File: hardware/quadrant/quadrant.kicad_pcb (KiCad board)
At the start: 4 copper layers, 216 x 200 mm, 68 parts, among them J1 FPC 16, P1 NPTH

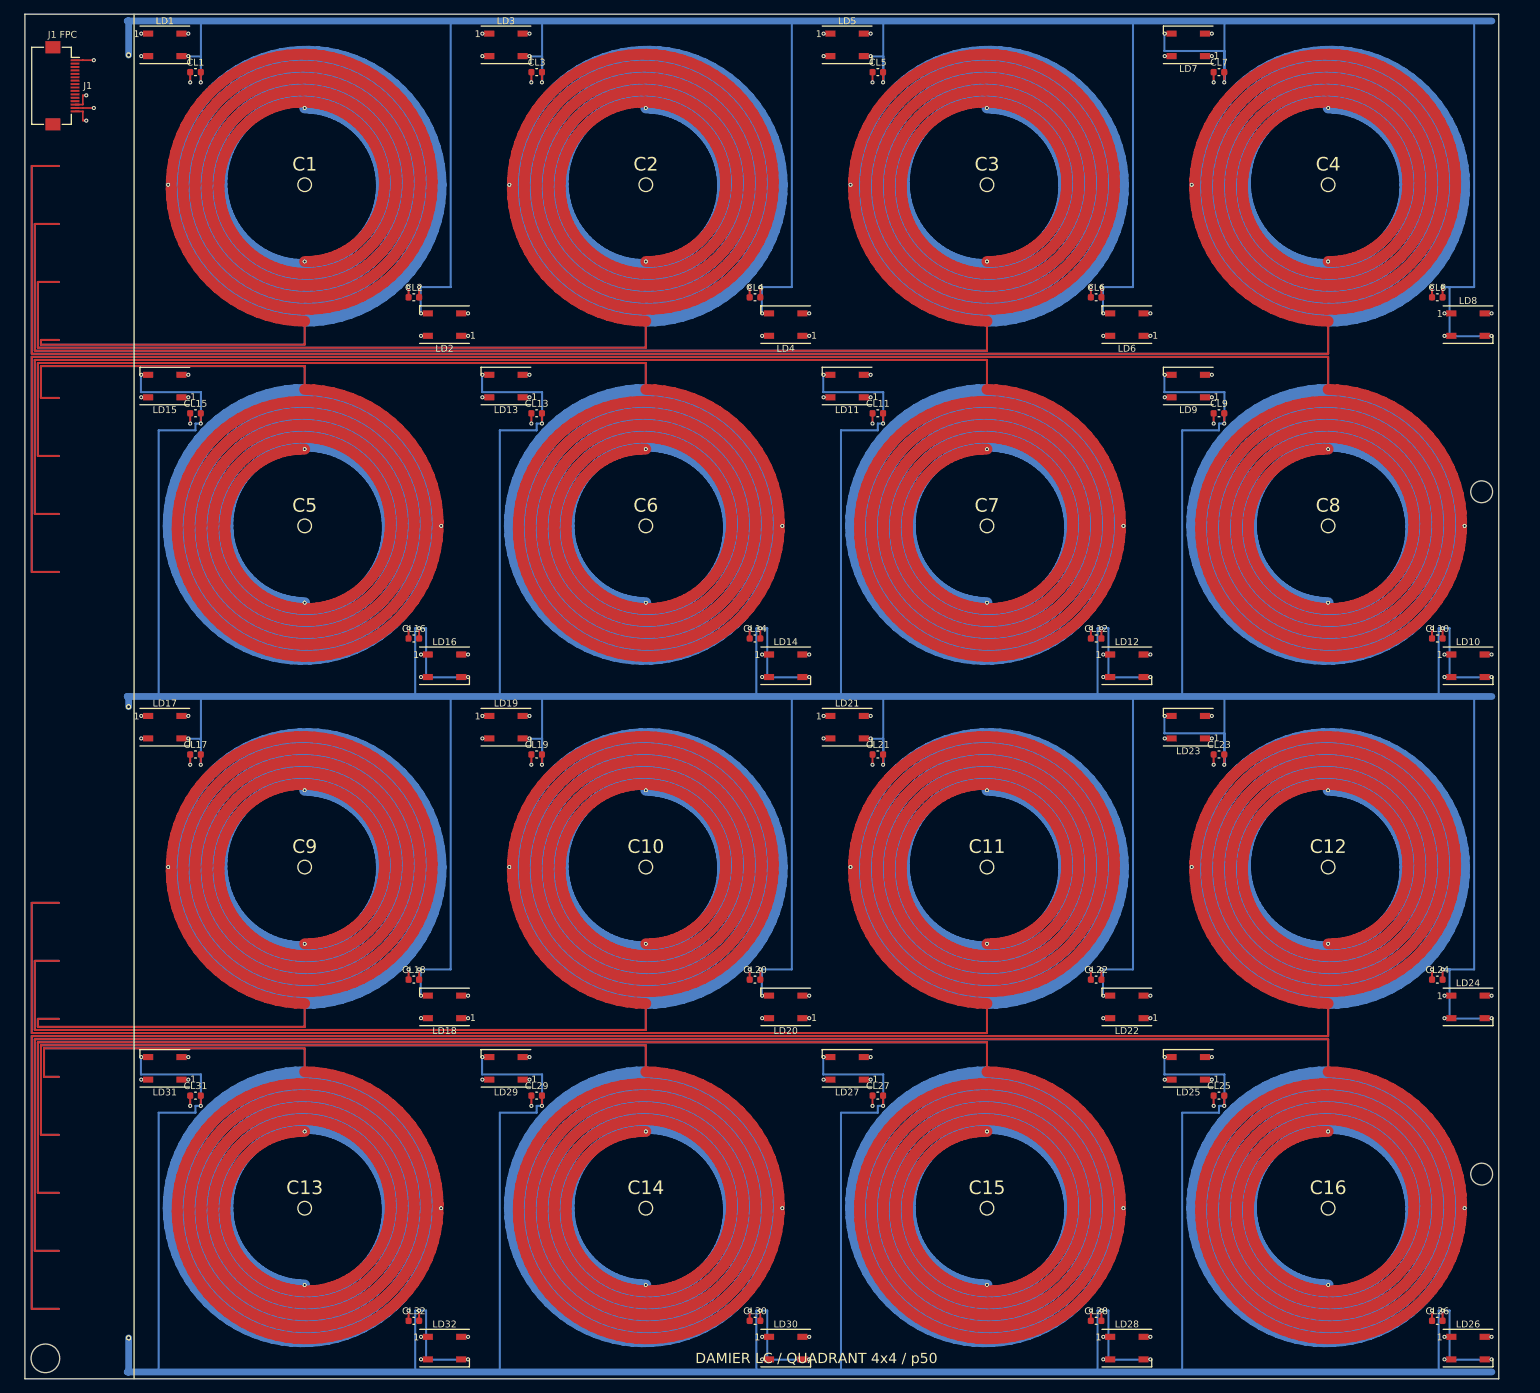
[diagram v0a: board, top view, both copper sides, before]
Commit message: Frontal du quadrant, cinq cartes generees, firmware cerveau et ESP32, protocole
Quadrant : frontal complet (16 cellules, deux ADG1607, decodeurs
74HC4514 et 74HC154, inverseur, chaine AD8421 et OPA2810, FPC 16
broches) place et route par le routeur A* multicouche ; sorties des
boitiers fins par eventail (troncon, via 0,45 mm sur deux rangees,
couloir de sortie), bandes d'echappee, controle d'isolement exact a
chaque route, zone du milieu en une colonne.

Generateur generique boardgen : cerveau STM32G474 quatre couches
(buck 2,5 MHz, LDO analogique, ADuM1201, ESP32-S3, embase Pi), carte
puissance (BQ24610, BQ76920, INA219), carte moteurs (deux TMC2209),
carte horloge (ESP32-S3, MCP73831, 18650, ecran, barre a bascule) ;
projets KiCad, BOM et CPL dans hardware/, rendus dans docs/images.

Firmware du cerveau (quatre quadrants par le bus de mux, quatre ADC,
128 LED), pont radio et horloge en ESP-IDF avec logique de pendule
testee sur PC, protocole texte commun (note 12). Notes 07, 09, 10,
11 et 12, README des cartes, CI (firmware cerveau, test de l'horloge).
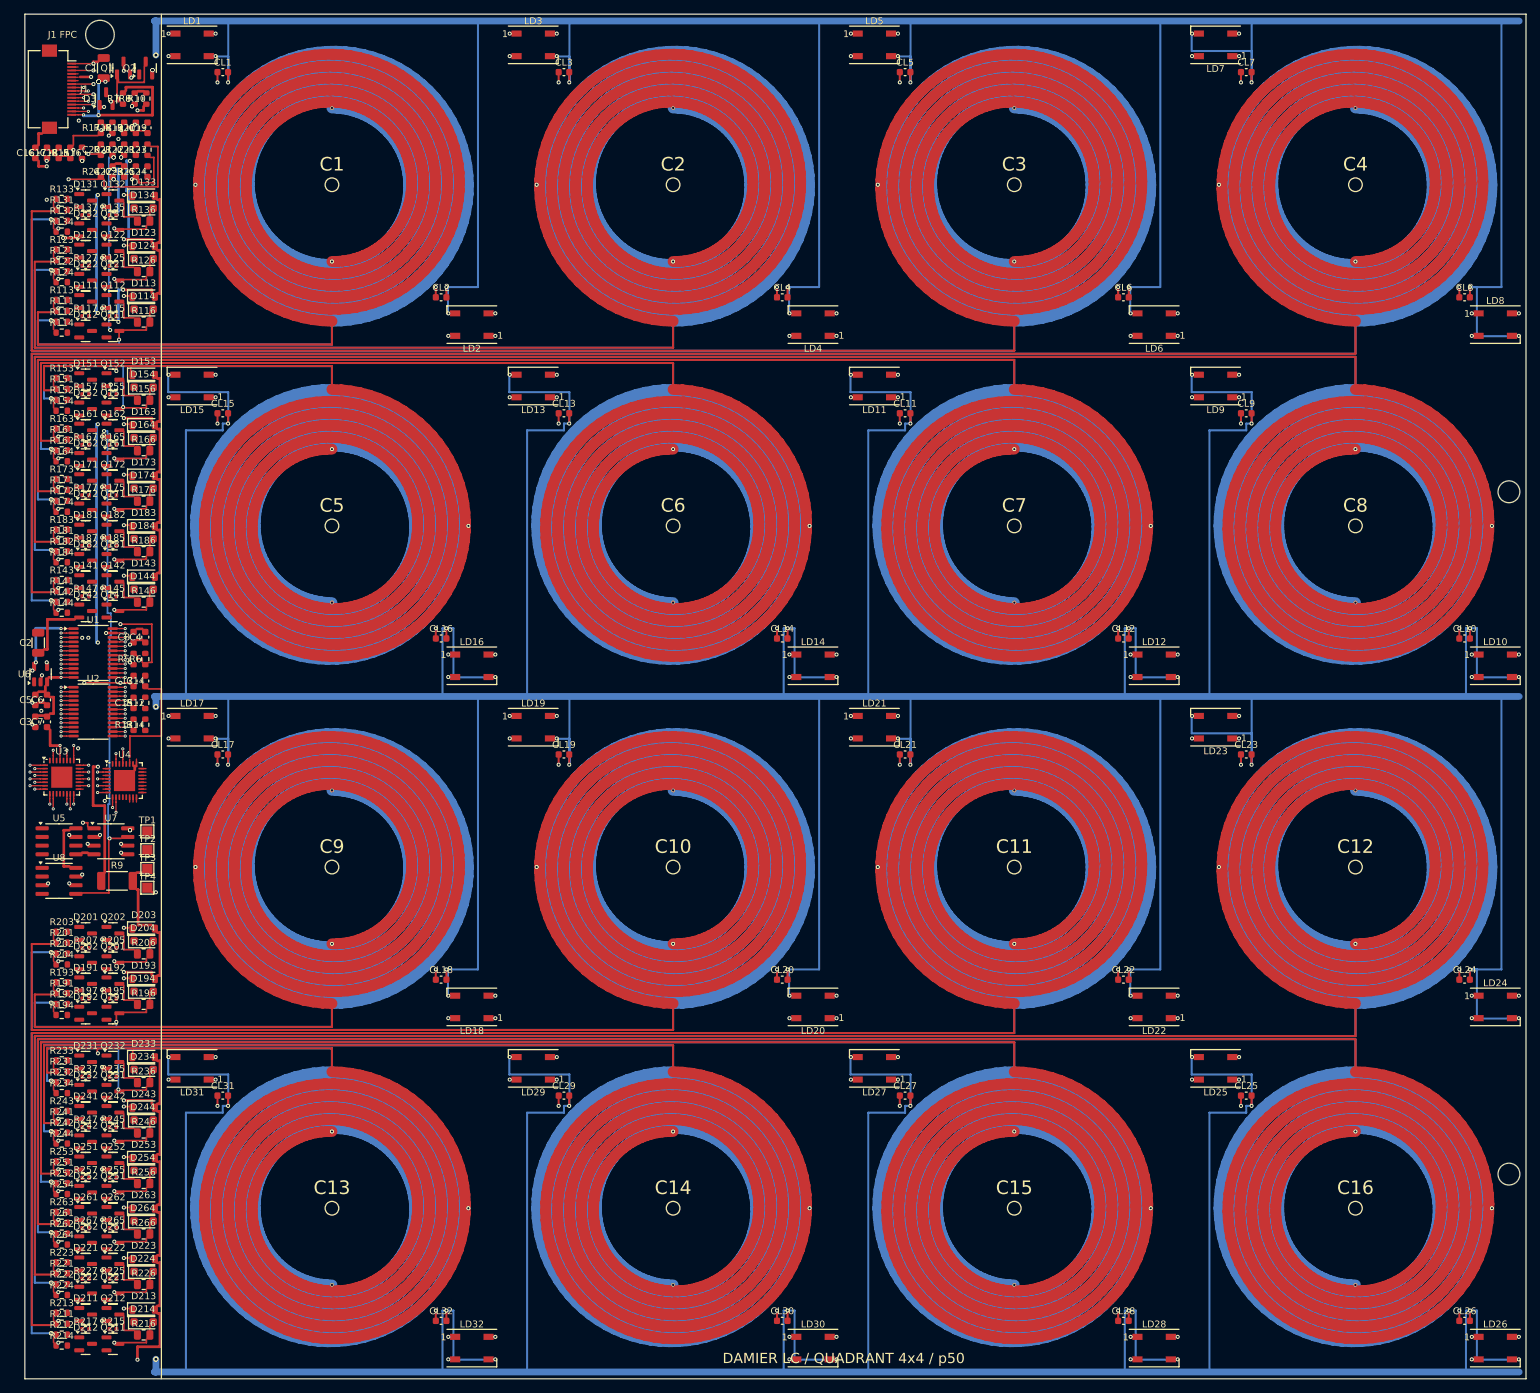
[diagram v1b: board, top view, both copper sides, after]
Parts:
- added C1: 10u/25V, Capacitor_SMD:C_1206_3216Metric, F.Cu at (11.6, 7.90)
- added C13: 1u, Capacitor_SMD:C_0603_1608Metric, F.Cu at (15.9, 97.7)
- added C14: 100n, Capacitor_SMD:C_0603_1608Metric, F.Cu at (17.6, 97.7)
- added C15: 100n, Capacitor_SMD:C_0603_1608Metric, F.Cu at (15.9, 100.9)
- added C16: 100n, Capacitor_SMD:C_0603_1608Metric, F.Cu at (1.53, 20.3)
- added C17: 1n, Capacitor_SMD:C_0603_1608Metric, F.Cu at (3.24, 20.3)
- added C18: 1n, Capacitor_SMD:C_0603_1608Metric, F.Cu at (4.95, 20.3)
- added C19: 330p, Capacitor_SMD:C_0603_1608Metric, F.Cu at (18.0, 16.7)
- added C2: 10u/10V, Capacitor_SMD:C_1206_3216Metric, F.Cu at (1.95, 92.1)
- added C20: 330p, Capacitor_SMD:C_0603_1608Metric, F.Cu at (11.1, 19.9)
- added C21: 100n, Capacitor_SMD:C_0603_1608Metric, F.Cu at (16.3, 19.9)
- added C22: 100n, Capacitor_SMD:C_0603_1608Metric, F.Cu at (12.8, 23.1)
- added C23: 1u, Capacitor_SMD:C_0603_1608Metric, F.Cu at (14.6, 23.1)
- added C24: 1n, Capacitor_SMD:C_0603_1608Metric, F.Cu at (18.0, 23.1)
- added C3: 100n, Capacitor_SMD:C_0603_1608Metric, F.Cu at (1.53, 103.7)
- added C4: 100n, Capacitor_SMD:C_0603_1608Metric, F.Cu at (17.6, 91.3)
- added C5: 100n, Capacitor_SMD:C_0603_1608Metric, F.Cu at (1.53, 100.5)
- added C6: 100n, Capacitor_SMD:C_0603_1608Metric, F.Cu at (3.24, 100.5)
- added C7: 100n, Capacitor_SMD:C_0603_1608Metric, F.Cu at (3.24, 103.7)
- added C8: 100n, Capacitor_SMD:C_0603_1608Metric, F.Cu at (15.9, 91.3)
- added D111: BAV99, Package_TO_SOT_SMD:SOT-23, F.Cu at (8.90, 42.1)
- added D112: BAV99, Package_TO_SOT_SMD:SOT-23, F.Cu at (8.90, 46.4)
- added D113: B5819W, Diode_SMD:D_SOD-123, F.Cu at (17.4, 41.4)
- added D114: SS34FL, Diode_SMD:D_SOD-123F, F.Cu at (17.4, 43.2)
- added D121: BAV99, Package_TO_SOT_SMD:SOT-23, F.Cu at (8.90, 34.7)
- added D122: BAV99, Package_TO_SOT_SMD:SOT-23, F.Cu at (8.90, 39.0)
- added D123: B5819W, Diode_SMD:D_SOD-123, F.Cu at (17.4, 34.0)
- added D124: SS34FL, Diode_SMD:D_SOD-123F, F.Cu at (17.4, 35.8)
- added D131: BAV99, Package_TO_SOT_SMD:SOT-23, F.Cu at (8.90, 27.3)
- added D132: BAV99, Package_TO_SOT_SMD:SOT-23, F.Cu at (8.90, 31.6)
- added D133: B5819W, Diode_SMD:D_SOD-123, F.Cu at (17.4, 26.6)
- added D134: SS34FL, Diode_SMD:D_SOD-123F, F.Cu at (17.4, 28.4)
- added D141: BAV99, Package_TO_SOT_SMD:SOT-23, F.Cu at (8.90, 83.2)
- added D142: BAV99, Package_TO_SOT_SMD:SOT-23, F.Cu at (8.90, 87.5)
- added D143: B5819W, Diode_SMD:D_SOD-123, F.Cu at (17.4, 82.5)
- added D144: SS34FL, Diode_SMD:D_SOD-123F, F.Cu at (17.4, 84.3)
- added D151: BAV99, Package_TO_SOT_SMD:SOT-23, F.Cu at (8.90, 53.6)
- added D152: BAV99, Package_TO_SOT_SMD:SOT-23, F.Cu at (8.90, 57.9)
- added D153: B5819W, Diode_SMD:D_SOD-123, F.Cu at (17.4, 52.9)
- added D154: SS34FL, Diode_SMD:D_SOD-123F, F.Cu at (17.4, 54.7)
- added D161: BAV99, Package_TO_SOT_SMD:SOT-23, F.Cu at (8.90, 61.0)
- added D162: BAV99, Package_TO_SOT_SMD:SOT-23, F.Cu at (8.90, 65.3)
- added D163: B5819W, Diode_SMD:D_SOD-123, F.Cu at (17.4, 60.3)
- added D164: SS34FL, Diode_SMD:D_SOD-123F, F.Cu at (17.4, 62.1)
- added D171: BAV99, Package_TO_SOT_SMD:SOT-23, F.Cu at (8.90, 68.4)
- added D172: BAV99, Package_TO_SOT_SMD:SOT-23, F.Cu at (8.90, 72.7)
- added D173: B5819W, Diode_SMD:D_SOD-123, F.Cu at (17.4, 67.7)
- added D174: SS34FL, Diode_SMD:D_SOD-123F, F.Cu at (17.4, 69.5)
- added D181: BAV99, Package_TO_SOT_SMD:SOT-23, F.Cu at (8.90, 75.8)
- added D182: BAV99, Package_TO_SOT_SMD:SOT-23, F.Cu at (8.90, 80.1)
- added D183: B5819W, Diode_SMD:D_SOD-123, F.Cu at (17.4, 75.1)
- added D184: SS34FL, Diode_SMD:D_SOD-123F, F.Cu at (17.4, 76.9)
- added D191: BAV99, Package_TO_SOT_SMD:SOT-23, F.Cu at (8.90, 142.1)
- added D192: BAV99, Package_TO_SOT_SMD:SOT-23, F.Cu at (8.90, 146.4)
- added D193: B5819W, Diode_SMD:D_SOD-123, F.Cu at (17.4, 141.4)
- added D194: SS34FL, Diode_SMD:D_SOD-123F, F.Cu at (17.4, 143.2)
- added D201: BAV99, Package_TO_SOT_SMD:SOT-23, F.Cu at (8.90, 134.7)
- added D202: BAV99, Package_TO_SOT_SMD:SOT-23, F.Cu at (8.90, 139.0)
- added D203: B5819W, Diode_SMD:D_SOD-123, F.Cu at (17.4, 134.0)
- added D204: SS34FL, Diode_SMD:D_SOD-123F, F.Cu at (17.4, 135.8)
- added D211: BAV99, Package_TO_SOT_SMD:SOT-23, F.Cu at (8.90, 190.6)
- added D212: BAV99, Package_TO_SOT_SMD:SOT-23, F.Cu at (8.90, 194.9)
- added D213: B5819W, Diode_SMD:D_SOD-123, F.Cu at (17.4, 189.9)
- added D214: SS34FL, Diode_SMD:D_SOD-123F, F.Cu at (17.4, 191.7)
- added D221: BAV99, Package_TO_SOT_SMD:SOT-23, F.Cu at (8.90, 183.2)
- added D222: BAV99, Package_TO_SOT_SMD:SOT-23, F.Cu at (8.90, 187.5)
- added D223: B5819W, Diode_SMD:D_SOD-123, F.Cu at (17.4, 182.5)
- added D224: SS34FL, Diode_SMD:D_SOD-123F, F.Cu at (17.4, 184.3)
- added D231: BAV99, Package_TO_SOT_SMD:SOT-23, F.Cu at (8.90, 153.6)
- added D232: BAV99, Package_TO_SOT_SMD:SOT-23, F.Cu at (8.90, 157.9)
- added D233: B5819W, Diode_SMD:D_SOD-123, F.Cu at (17.4, 152.9)
- added D234: SS34FL, Diode_SMD:D_SOD-123F, F.Cu at (17.4, 154.7)
- added D241: BAV99, Package_TO_SOT_SMD:SOT-23, F.Cu at (8.90, 161.0)
- added D242: BAV99, Package_TO_SOT_SMD:SOT-23, F.Cu at (8.90, 165.3)
- added D243: B5819W, Diode_SMD:D_SOD-123, F.Cu at (17.4, 160.3)
- added D244: SS34FL, Diode_SMD:D_SOD-123F, F.Cu at (17.4, 162.1)
- added D251: BAV99, Package_TO_SOT_SMD:SOT-23, F.Cu at (8.90, 168.4)
- added D252: BAV99, Package_TO_SOT_SMD:SOT-23, F.Cu at (8.90, 172.7)
- added D253: B5819W, Diode_SMD:D_SOD-123, F.Cu at (17.4, 167.7)
- added D254: SS34FL, Diode_SMD:D_SOD-123F, F.Cu at (17.4, 169.5)
- added D261: BAV99, Package_TO_SOT_SMD:SOT-23, F.Cu at (8.90, 175.8)
- added D262: BAV99, Package_TO_SOT_SMD:SOT-23, F.Cu at (8.90, 180.1)
- added D263: B5819W, Diode_SMD:D_SOD-123, F.Cu at (17.4, 175.1)
- added D264: SS34FL, Diode_SMD:D_SOD-123F, F.Cu at (17.4, 176.9)
- added D3: BAV99, Package_TO_SOT_SMD:SOT-23, F.Cu at (11.9, 12.4)
- added NT1: spirale, quadgen:COIL_TIE, F.Cu at (45.0, 13.8)
- added NT10: spirale, quadgen:COIL_TIE, F.Cu at (95.0, 113.8)
- added NT11: spirale, quadgen:COIL_TIE, F.Cu at (145.0, 113.8)
- added NT12: spirale, quadgen:COIL_TIE, F.Cu at (195.0, 113.8)
- added NT13: spirale, quadgen:COIL_TIE, F.Cu at (45.0, 186.2)
- added NT14: spirale, quadgen:COIL_TIE, F.Cu at (95.0, 186.2)
- added NT15: spirale, quadgen:COIL_TIE, F.Cu at (145.0, 186.2)
- added NT16: spirale, quadgen:COIL_TIE, F.Cu at (195.0, 186.2)
- added NT2: spirale, quadgen:COIL_TIE, F.Cu at (95.0, 13.8)
- added NT3: spirale, quadgen:COIL_TIE, F.Cu at (145.0, 13.8)
- added NT4: spirale, quadgen:COIL_TIE, F.Cu at (195.0, 13.8)
- added NT5: spirale, quadgen:COIL_TIE, F.Cu at (45.0, 86.2)
- added NT6: spirale, quadgen:COIL_TIE, F.Cu at (95.0, 86.2)
- added NT7: spirale, quadgen:COIL_TIE, F.Cu at (145.0, 86.2)
- added NT8: spirale, quadgen:COIL_TIE, F.Cu at (195.0, 86.2)
- added NT9: spirale, quadgen:COIL_TIE, F.Cu at (45.0, 113.8)
- added Q1: AO3401A, Package_TO_SOT_SMD:SOT-23, F.Cu at (14.4, 7.90)
- added Q111: AO3400A, Package_TO_SOT_SMD:SOT-23, F.Cu at (12.9, 46.4)
- added Q112: AO3401A, Package_TO_SOT_SMD:SOT-23, F.Cu at (12.9, 42.1)
- added Q121: AO3400A, Package_TO_SOT_SMD:SOT-23, F.Cu at (12.9, 39.0)
- added Q122: AO3401A, Package_TO_SOT_SMD:SOT-23, F.Cu at (12.9, 34.7)
- added Q131: AO3400A, Package_TO_SOT_SMD:SOT-23, F.Cu at (12.9, 31.6)
- added Q132: AO3401A, Package_TO_SOT_SMD:SOT-23, F.Cu at (12.9, 27.3)
- added Q141: AO3400A, Package_TO_SOT_SMD:SOT-23, F.Cu at (12.9, 87.5)
- added Q142: AO3401A, Package_TO_SOT_SMD:SOT-23, F.Cu at (12.9, 83.2)
- added Q151: AO3400A, Package_TO_SOT_SMD:SOT-23, F.Cu at (12.9, 57.9)
- added Q152: AO3401A, Package_TO_SOT_SMD:SOT-23, F.Cu at (12.9, 53.6)
- added Q161: AO3400A, Package_TO_SOT_SMD:SOT-23, F.Cu at (12.9, 65.3)
- added Q162: AO3401A, Package_TO_SOT_SMD:SOT-23, F.Cu at (12.9, 61.0)
- added Q171: AO3400A, Package_TO_SOT_SMD:SOT-23, F.Cu at (12.9, 72.7)
- added Q172: AO3401A, Package_TO_SOT_SMD:SOT-23, F.Cu at (12.9, 68.4)
- added Q181: AO3400A, Package_TO_SOT_SMD:SOT-23, F.Cu at (12.9, 80.1)
- added Q182: AO3401A, Package_TO_SOT_SMD:SOT-23, F.Cu at (12.9, 75.8)
- added Q191: AO3400A, Package_TO_SOT_SMD:SOT-23, F.Cu at (12.9, 146.4)
- added Q192: AO3401A, Package_TO_SOT_SMD:SOT-23, F.Cu at (12.9, 142.1)
- added Q2: AO3400A, Package_TO_SOT_SMD:SOT-23, F.Cu at (17.7, 7.90)
- added Q201: AO3400A, Package_TO_SOT_SMD:SOT-23, F.Cu at (12.9, 139.0)
- added Q202: AO3401A, Package_TO_SOT_SMD:SOT-23, F.Cu at (12.9, 134.7)
- added Q211: AO3400A, Package_TO_SOT_SMD:SOT-23, F.Cu at (12.9, 194.9)
- added Q212: AO3401A, Package_TO_SOT_SMD:SOT-23, F.Cu at (12.9, 190.6)
- added Q221: AO3400A, Package_TO_SOT_SMD:SOT-23, F.Cu at (12.9, 187.5)
- added Q222: AO3401A, Package_TO_SOT_SMD:SOT-23, F.Cu at (12.9, 183.2)
- added Q231: AO3400A, Package_TO_SOT_SMD:SOT-23, F.Cu at (12.9, 157.9)
- added Q232: AO3401A, Package_TO_SOT_SMD:SOT-23, F.Cu at (12.9, 153.6)
- added Q241: AO3400A, Package_TO_SOT_SMD:SOT-23, F.Cu at (12.9, 165.3)
- added Q242: AO3401A, Package_TO_SOT_SMD:SOT-23, F.Cu at (12.9, 161.0)
- added Q251: AO3400A, Package_TO_SOT_SMD:SOT-23, F.Cu at (12.9, 172.7)
- added Q252: AO3401A, Package_TO_SOT_SMD:SOT-23, F.Cu at (12.9, 168.4)
- added Q261: AO3400A, Package_TO_SOT_SMD:SOT-23, F.Cu at (12.9, 180.1)
- added Q262: AO3401A, Package_TO_SOT_SMD:SOT-23, F.Cu at (12.9, 175.8)
- added R10: 100k, Resistor_SMD:R_0603_1608Metric, F.Cu at (17.8, 12.4)
- added R111: 10k, Resistor_SMD:R_0603_1608Metric, F.Cu at (5.40, 43.5)
- added R112: 10k, Resistor_SMD:R_0603_1608Metric, F.Cu at (5.40, 45.1)
- added R113: 330R, Resistor_SMD:R_0603_1608Metric, F.Cu at (5.40, 41.9)
- added R114: 330R, Resistor_SMD:R_0603_1608Metric, F.Cu at (5.40, 46.7)
- added R115: 100k, Resistor_SMD:R_0402_1005Metric, F.Cu at (12.9, 44.3)
- added R116: 680R, Resistor_SMD:R_0805_2012Metric, F.Cu at (17.4, 45.1)
- added R117: 100k, Resistor_SMD:R_0402_1005Metric, F.Cu at (8.90, 44.3)
- added R12: 100k, Resistor_SMD:R_0603_1608Metric, F.Cu at (17.6, 100.9)
- added R121: 10k, Resistor_SMD:R_0603_1608Metric, F.Cu at (5.40, 36.1)
- added R122: 10k, Resistor_SMD:R_0603_1608Metric, F.Cu at (5.40, 37.7)
- added R123: 330R, Resistor_SMD:R_0603_1608Metric, F.Cu at (5.40, 34.5)
- added R124: 330R, Resistor_SMD:R_0603_1608Metric, F.Cu at (5.40, 39.3)
- added R125: 100k, Resistor_SMD:R_0402_1005Metric, F.Cu at (12.9, 36.9)
- added R126: 680R, Resistor_SMD:R_0805_2012Metric, F.Cu at (17.4, 37.7)
- added R127: 100k, Resistor_SMD:R_0402_1005Metric, F.Cu at (8.90, 36.9)
- added R13: 100k, Resistor_SMD:R_0603_1608Metric, F.Cu at (15.9, 104.1)
- added R131: 10k, Resistor_SMD:R_0603_1608Metric, F.Cu at (5.40, 28.7)
- added R132: 10k, Resistor_SMD:R_0603_1608Metric, F.Cu at (5.40, 30.3)
- added R133: 330R, Resistor_SMD:R_0603_1608Metric, F.Cu at (5.40, 27.1)
- added R134: 330R, Resistor_SMD:R_0603_1608Metric, F.Cu at (5.40, 31.9)
- added R135: 100k, Resistor_SMD:R_0402_1005Metric, F.Cu at (12.9, 29.5)
- added R136: 680R, Resistor_SMD:R_0805_2012Metric, F.Cu at (17.4, 30.3)
- added R137: 100k, Resistor_SMD:R_0402_1005Metric, F.Cu at (8.90, 29.5)
- added R14: 523R, Resistor_SMD:R_0603_1608Metric, F.Cu at (17.6, 104.1)
- added R141: 10k, Resistor_SMD:R_0603_1608Metric, F.Cu at (5.40, 84.5)
- added R142: 10k, Resistor_SMD:R_0603_1608Metric, F.Cu at (5.40, 86.1)
- added R143: 330R, Resistor_SMD:R_0603_1608Metric, F.Cu at (5.40, 82.9)
- added R144: 330R, Resistor_SMD:R_0603_1608Metric, F.Cu at (5.40, 87.7)
- added R145: 100k, Resistor_SMD:R_0402_1005Metric, F.Cu at (12.9, 85.3)
- added R146: 680R, Resistor_SMD:R_0805_2012Metric, F.Cu at (17.4, 86.2)
- added R147: 100k, Resistor_SMD:R_0402_1005Metric, F.Cu at (8.90, 85.3)
- added R15: 787R, Resistor_SMD:R_0603_1608Metric, F.Cu at (6.66, 20.3)
- added R151: 10k, Resistor_SMD:R_0603_1608Metric, F.Cu at (5.40, 54.9)
- added R152: 10k, Resistor_SMD:R_0603_1608Metric, F.Cu at (5.40, 56.5)
- added R153: 330R, Resistor_SMD:R_0603_1608Metric, F.Cu at (5.40, 53.3)
- added R154: 330R, Resistor_SMD:R_0603_1608Metric, F.Cu at (5.40, 58.1)
- added R155: 100k, Resistor_SMD:R_0402_1005Metric, F.Cu at (12.9, 55.7)
- added R156: 680R, Resistor_SMD:R_0805_2012Metric, F.Cu at (17.4, 56.6)
- added R157: 100k, Resistor_SMD:R_0402_1005Metric, F.Cu at (8.90, 55.7)
- added R16: 787R, Resistor_SMD:R_0603_1608Metric, F.Cu at (8.37, 20.3)
- added R161: 10k, Resistor_SMD:R_0603_1608Metric, F.Cu at (5.40, 62.3)
- added R162: 10k, Resistor_SMD:R_0603_1608Metric, F.Cu at (5.40, 63.9)
- added R163: 330R, Resistor_SMD:R_0603_1608Metric, F.Cu at (5.40, 60.7)
- added R164: 330R, Resistor_SMD:R_0603_1608Metric, F.Cu at (5.40, 65.5)
- added R165: 100k, Resistor_SMD:R_0402_1005Metric, F.Cu at (12.9, 63.1)
- added R166: 680R, Resistor_SMD:R_0805_2012Metric, F.Cu at (17.4, 64.0)
- added R167: 100k, Resistor_SMD:R_0402_1005Metric, F.Cu at (8.90, 63.1)
- added R17: 590R, Resistor_SMD:R_0603_1608Metric, F.Cu at (11.1, 16.7)
- added R171: 10k, Resistor_SMD:R_0603_1608Metric, F.Cu at (5.40, 69.7)
- added R172: 10k, Resistor_SMD:R_0603_1608Metric, F.Cu at (5.40, 71.3)
- added R173: 330R, Resistor_SMD:R_0603_1608Metric, F.Cu at (5.40, 68.1)
- added R174: 330R, Resistor_SMD:R_0603_1608Metric, F.Cu at (5.40, 72.9)
- added R175: 100k, Resistor_SMD:R_0402_1005Metric, F.Cu at (12.9, 70.5)
- added R176: 680R, Resistor_SMD:R_0805_2012Metric, F.Cu at (17.4, 71.4)
- added R177: 100k, Resistor_SMD:R_0402_1005Metric, F.Cu at (8.90, 70.5)
- added R18: 1k, Resistor_SMD:R_0603_1608Metric, F.Cu at (12.8, 16.7)
- added R181: 10k, Resistor_SMD:R_0603_1608Metric, F.Cu at (5.40, 77.1)
- added R182: 10k, Resistor_SMD:R_0603_1608Metric, F.Cu at (5.40, 78.7)
- added R183: 330R, Resistor_SMD:R_0603_1608Metric, F.Cu at (5.40, 75.5)
- added R184: 330R, Resistor_SMD:R_0603_1608Metric, F.Cu at (5.40, 80.3)
- added R185: 100k, Resistor_SMD:R_0402_1005Metric, F.Cu at (12.9, 77.9)
- added R186: 680R, Resistor_SMD:R_0805_2012Metric, F.Cu at (17.4, 78.8)
- added R187: 100k, Resistor_SMD:R_0402_1005Metric, F.Cu at (8.90, 77.9)
- added R19: 750R, Resistor_SMD:R_0603_1608Metric, F.Cu at (14.6, 16.7)
- added R191: 10k, Resistor_SMD:R_0603_1608Metric, F.Cu at (5.40, 143.5)
- added R192: 10k, Resistor_SMD:R_0603_1608Metric, F.Cu at (5.40, 145.1)
- added R193: 330R, Resistor_SMD:R_0603_1608Metric, F.Cu at (5.40, 141.9)
- added R194: 330R, Resistor_SMD:R_0603_1608Metric, F.Cu at (5.40, 146.7)
- added R195: 100k, Resistor_SMD:R_0402_1005Metric, F.Cu at (12.9, 144.3)
- added R196: 680R, Resistor_SMD:R_0805_2012Metric, F.Cu at (17.4, 145.1)
- added R197: 100k, Resistor_SMD:R_0402_1005Metric, F.Cu at (8.90, 144.3)
- added R20: 750R, Resistor_SMD:R_0603_1608Metric, F.Cu at (16.3, 16.7)
- added R201: 10k, Resistor_SMD:R_0603_1608Metric, F.Cu at (5.40, 136.1)
- added R202: 10k, Resistor_SMD:R_0603_1608Metric, F.Cu at (5.40, 137.7)
- added R203: 330R, Resistor_SMD:R_0603_1608Metric, F.Cu at (5.40, 134.5)
- added R204: 330R, Resistor_SMD:R_0603_1608Metric, F.Cu at (5.40, 139.3)
- added R205: 100k, Resistor_SMD:R_0402_1005Metric, F.Cu at (12.9, 136.9)
- added R206: 680R, Resistor_SMD:R_0805_2012Metric, F.Cu at (17.4, 137.7)
- added R207: 100k, Resistor_SMD:R_0402_1005Metric, F.Cu at (8.90, 136.9)
- added R21: 590R, Resistor_SMD:R_0603_1608Metric, F.Cu at (12.8, 19.9)
- added R211: 10k, Resistor_SMD:R_0603_1608Metric, F.Cu at (5.40, 191.9)
- added R212: 10k, Resistor_SMD:R_0603_1608Metric, F.Cu at (5.40, 193.5)
- added R213: 330R, Resistor_SMD:R_0603_1608Metric, F.Cu at (5.40, 190.3)
- added R214: 330R, Resistor_SMD:R_0603_1608Metric, F.Cu at (5.40, 195.1)
- added R215: 100k, Resistor_SMD:R_0402_1005Metric, F.Cu at (12.9, 192.7)
- added R216: 680R, Resistor_SMD:R_0805_2012Metric, F.Cu at (17.4, 193.6)
- added R217: 100k, Resistor_SMD:R_0402_1005Metric, F.Cu at (8.90, 192.7)
- added R22: 1k, Resistor_SMD:R_0603_1608Metric, F.Cu at (14.6, 19.9)
- added R221: 10k, Resistor_SMD:R_0603_1608Metric, F.Cu at (5.40, 184.5)
- added R222: 10k, Resistor_SMD:R_0603_1608Metric, F.Cu at (5.40, 186.1)
- added R223: 330R, Resistor_SMD:R_0603_1608Metric, F.Cu at (5.40, 182.9)
- added R224: 330R, Resistor_SMD:R_0603_1608Metric, F.Cu at (5.40, 187.7)
- added R225: 100k, Resistor_SMD:R_0402_1005Metric, F.Cu at (12.9, 185.3)
- added R226: 680R, Resistor_SMD:R_0805_2012Metric, F.Cu at (17.4, 186.2)
- added R227: 100k, Resistor_SMD:R_0402_1005Metric, F.Cu at (8.90, 185.3)
- added R23: 3.57k, Resistor_SMD:R_0603_1608Metric, F.Cu at (18.0, 19.9)
- added R231: 10k, Resistor_SMD:R_0603_1608Metric, F.Cu at (5.40, 154.9)
- added R232: 10k, Resistor_SMD:R_0603_1608Metric, F.Cu at (5.40, 156.5)
- added R233: 330R, Resistor_SMD:R_0603_1608Metric, F.Cu at (5.40, 153.3)
- added R234: 330R, Resistor_SMD:R_0603_1608Metric, F.Cu at (5.40, 158.1)
- added R235: 100k, Resistor_SMD:R_0402_1005Metric, F.Cu at (12.9, 155.7)
- added R236: 680R, Resistor_SMD:R_0805_2012Metric, F.Cu at (17.4, 156.6)
- added R237: 100k, Resistor_SMD:R_0402_1005Metric, F.Cu at (8.90, 155.7)
- added R24: 1k, Resistor_SMD:R_0603_1608Metric, F.Cu at (11.1, 23.1)
- added R241: 10k, Resistor_SMD:R_0603_1608Metric, F.Cu at (5.40, 162.3)
- added R242: 10k, Resistor_SMD:R_0603_1608Metric, F.Cu at (5.40, 163.9)
- added R243: 330R, Resistor_SMD:R_0603_1608Metric, F.Cu at (5.40, 160.7)
- added R244: 330R, Resistor_SMD:R_0603_1608Metric, F.Cu at (5.40, 165.5)
- added R245: 100k, Resistor_SMD:R_0402_1005Metric, F.Cu at (12.9, 163.1)
- added R246: 680R, Resistor_SMD:R_0805_2012Metric, F.Cu at (17.4, 164.0)
- added R247: 100k, Resistor_SMD:R_0402_1005Metric, F.Cu at (8.90, 163.1)
- added R25: 49R9, Resistor_SMD:R_0603_1608Metric, F.Cu at (16.3, 23.1)
- added R251: 10k, Resistor_SMD:R_0603_1608Metric, F.Cu at (5.40, 169.7)
- added R252: 10k, Resistor_SMD:R_0603_1608Metric, F.Cu at (5.40, 171.3)
- added R253: 330R, Resistor_SMD:R_0603_1608Metric, F.Cu at (5.40, 168.1)
- added R254: 330R, Resistor_SMD:R_0603_1608Metric, F.Cu at (5.40, 172.9)
- added R255: 100k, Resistor_SMD:R_0402_1005Metric, F.Cu at (12.9, 170.5)
- added R256: 680R, Resistor_SMD:R_0805_2012Metric, F.Cu at (17.4, 171.4)
- added R257: 100k, Resistor_SMD:R_0402_1005Metric, F.Cu at (8.90, 170.5)
- added R261: 10k, Resistor_SMD:R_0603_1608Metric, F.Cu at (5.40, 177.1)
- added R262: 10k, Resistor_SMD:R_0603_1608Metric, F.Cu at (5.40, 178.7)
- added R263: 330R, Resistor_SMD:R_0603_1608Metric, F.Cu at (5.40, 175.5)
- added R264: 330R, Resistor_SMD:R_0603_1608Metric, F.Cu at (5.40, 180.3)
- added R265: 100k, Resistor_SMD:R_0402_1005Metric, F.Cu at (12.9, 177.9)
- added R266: 680R, Resistor_SMD:R_0805_2012Metric, F.Cu at (17.4, 178.8)
- added R267: 100k, Resistor_SMD:R_0402_1005Metric, F.Cu at (8.90, 177.9)
- added R5: 20k5, Resistor_SMD:R_0603_1608Metric, F.Cu at (15.9, 94.5)
- added R6: 10k, Resistor_SMD:R_0603_1608Metric, F.Cu at (17.6, 94.5)
- added R7: 10k, Resistor_SMD:R_0603_1608Metric, F.Cu at (14.4, 12.4)
- added R8: 100k, Resistor_SMD:R_0603_1608Metric, F.Cu at (16.1, 12.4)
- added R9: 10R, Resistor_SMD:R_2010_5025Metric, F.Cu at (13.5, 127.0)
- added TP1: AMP_OUT, TestPoint:TestPoint_Pad_1.5x1.5mm, F.Cu at (17.9, 119.8)
- added TP2: VREF, TestPoint:TestPoint_Pad_1.5x1.5mm, F.Cu at (17.9, 122.5)
- added TP3: DRIVE_BUS, TestPoint:TestPoint_Pad_1.5x1.5mm, F.Cu at (17.9, 125.3)
- added TP4: GND, TestPoint:TestPoint_Pad_1.5x1.5mm, F.Cu at (17.9, 128.0)
- added U1: 74HC4514, Package_SO:TSSOP-24_4.4x7.8mm_P0.65mm, F.Cu at (10.0, 93.6)
- added U2: 74HC154, Package_SO:TSSOP-24_4.4x7.8mm_P0.65mm, F.Cu at (10.0, 102.2)
- added U3: ADG1607, Package_CSP:LFCSP-32-1EP_5x5mm_P0.5mm_EP3.1x3.1mm, F.Cu at (5.40, 111.8)
- added U4: ADG1607, Package_CSP:LFCSP-32-1EP_5x5mm_P0.5mm_EP3.1x3.1mm, F.Cu at (14.6, 112.3)
- added U5: AD8421, Package_SO:SOIC-8_3.9x4.9mm_P1.27mm, F.Cu at (5.00, 121.2)
- added U6: 74LVC1G04, Package_TO_SOT_SMD:SOT-23-5, F.Cu at (2.30, 96.7)
- added U7: OPA2810, Package_SO:SOIC-8_3.9x4.9mm_P1.27mm, F.Cu at (12.6, 121.2)
- added U8: OPA2810, Package_SO:SOIC-8_3.9x4.9mm_P1.27mm, F.Cu at (5.00, 127.0)
- moved P1 194.2 mm to (11.0, 3.00)
- moved CL1 4.00 mm to (29.0, 8.50)
- moved CL10 4.00 mm to (211.0, 91.5)
- moved CL11 4.00 mm to (129.0, 58.5)
- moved CL12 4.00 mm to (161.0, 91.5)
- moved CL13 4.00 mm to (79.0, 58.5)
- moved CL14 4.00 mm to (111.0, 91.5)
- moved CL15 4.00 mm to (29.0, 58.5)
- moved CL16 4.00 mm to (61.0, 91.5)
- moved CL17 4.00 mm to (29.0, 108.5)
- moved CL18 4.00 mm to (61.0, 141.5)
- moved CL19 4.00 mm to (79.0, 108.5)
- moved CL2 4.00 mm to (61.0, 41.5)
- moved CL20 4.00 mm to (111.0, 141.5)
- moved CL21 4.00 mm to (129.0, 108.5)
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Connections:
- J1 pad 10: MUX_EN -> 5V_LED
- J1 pad 11: PULSE_EN -> MUX_EN_L
- J1 pad 12: DAMP_EN -> MUX_EN_H
- J1 pad 13: VIN -> LED_DOUT
- J1 pad 14: 5V_LED -> PULSE_EN
- J1 pad 15: LED_DIN -> DAMP_EN_N
- J1 pad 16: LED_DOUT -> VIN
- J1 pad 3: AGND -> GND
- J1 pad 7: MUX_A1 -> LED_DIN
- J1 pad 8: MUX_A2 -> MUX_A1
- J1 pad 9: MUX_A3 -> MUX_A2
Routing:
- net C12: track 2539.1 -> 0.00 mm, vias 3 -> 0
- net C8: track 2522.2 -> 0.00 mm, vias 3 -> 0
- net C16: track 2519.4 -> 0.00 mm, vias 3 -> 0
- net C4: track 2514.2 -> 0.00 mm, vias 3 -> 0
- net C7: track 2401.6 -> 0.00 mm, vias 3 -> 0
- net C15: track 2398.8 -> 0.00 mm, vias 3 -> 0
- net C11: track 2396.4 -> 0.00 mm, vias 3 -> 0
- net C3: track 2393.6 -> 0.00 mm, vias 3 -> 0
- net C6: track 2281.0 -> 0.00 mm, vias 3 -> 0
- net C14: track 2278.2 -> 0.00 mm, vias 3 -> 0
- net C10: track 2275.8 -> 0.00 mm, vias 3 -> 0
- net C2: track 2273.0 -> 0.00 mm, vias 3 -> 0
- net C5: track 2160.4 -> 0.00 mm, vias 3 -> 0
- net C13: track 2157.6 -> 0.00 mm, vias 3 -> 0
- net C9: track 2155.2 -> 0.00 mm, vias 3 -> 0
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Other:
- board size 216 x 200 mm -> 220 x 200 mm

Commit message: Quadrant régénéré avec les bobines corrigées ; pastilles libres bloquantes pour le routeur
Le routeur du frontal ignorait les pastilles non connectées (NC des
mux) et y faisait passer une piste de masse : toute pastille libre est
désormais un obstacle dans le routeur et dans les contrôles. Quadrant
régénéré avec les vias d'empilement décalées et le net tie dans le
creux ; note 14 complétée.
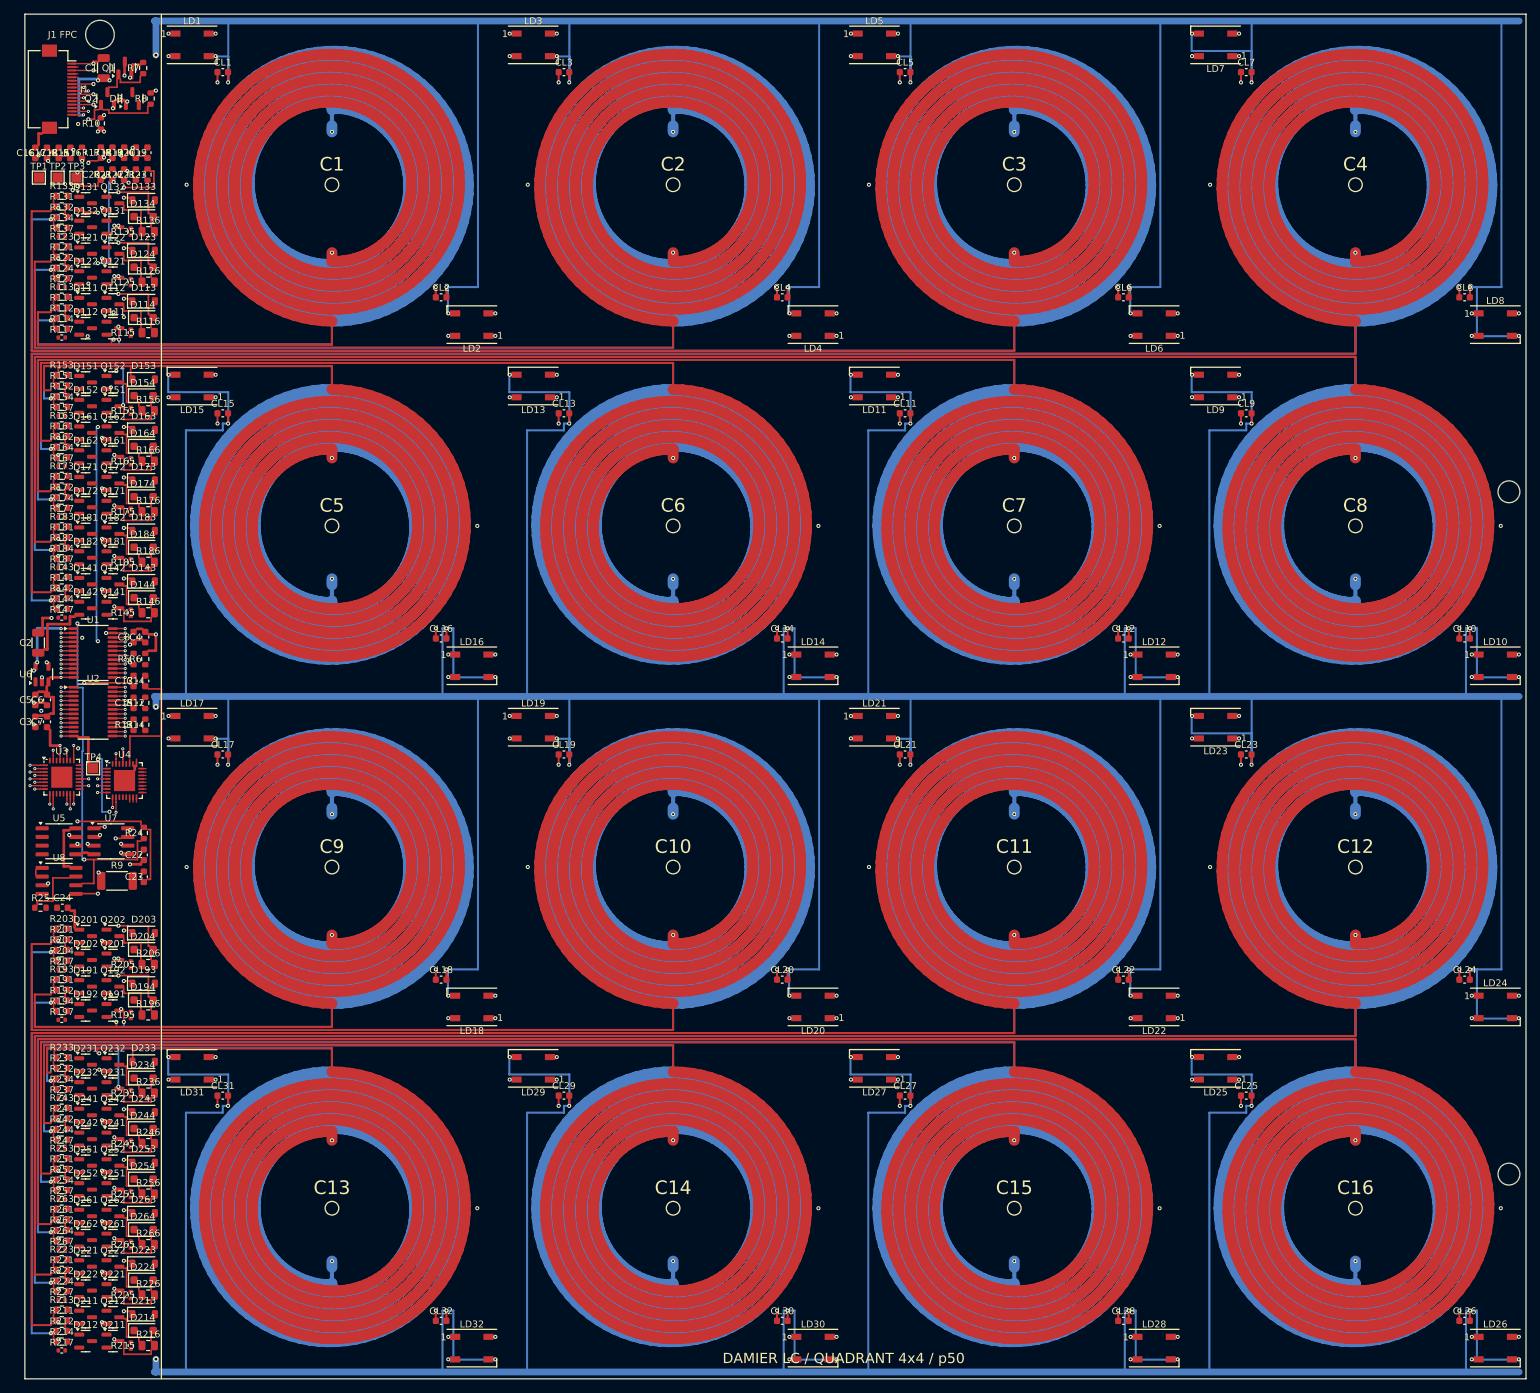
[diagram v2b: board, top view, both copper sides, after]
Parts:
- moved R25 108.8 mm to (2.28, 131.0), turned to 0 degrees
- moved C24 108.6 mm to (5.49, 131.0), turned to 0 degrees
- moved C23 103.4 mm to (17.4, 126.4)
- moved TP3 101.9 mm to (7.55, 23.9)
- moved C22 100.2 mm to (17.4, 123.2)
- moved TP2 99.4 mm to (4.80, 23.9)
- moved TP1 97.1 mm to (2.05, 23.9)
- moved R24 97.1 mm to (17.4, 120.0)
- moved TP4 19.2 mm to (10.0, 110.5)
- moved R10 7.60 mm to (11.1, 16.0)
- moved Q2 7.17 mm to (12.1, 12.4)
- moved R7 5.36 mm to (17.3, 7.90)
- moved R117 4.69 mm to (5.40, 47.4)
- moved R167 4.69 mm to (5.40, 66.2)
- moved R187 4.69 mm to (5.40, 81.0)
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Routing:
- net DRIVE_BUS: track 373.2 -> 193.7 mm, vias 9 -> 3
- net OUT_STAGE: track 119.4 -> 8.60 mm, vias 2 -> 0
- net VREF: track 170.7 -> 208.6 mm, vias 0 -> 3
- net VREF_DIV: track 64.4 -> 41.8 mm, vias 4 -> 2
- net GND: track 2269.3 -> 2285.2 mm, vias 88 -> 81
- net PULSE_RAIL: track 125.7 -> 140.7 mm, vias 7 -> 4
- net VIN: track 200.6 -> 186.7 mm, vias 37 -> 4
- net 5VA: track 233.7 -> 221.5 mm, vias 11 -> 8
- net C5_A: track 1577.2 -> 1588.2 mm, vias 4 -> 5
- net C13_A: track 1576.2 -> 1587.2 mm, vias 4 -> 5
- net C9_B: track 600.2 -> 610.3 mm, vias 3 -> 4
- net C8_A: track 1762.7 -> 1772.4 mm, vias 5 -> 6
- net C10_A: track 1648.1 -> 1657.8 mm, vias 5 -> 6
- net C3_A: track 1706.4 -> 1716.1 mm, vias 5 -> 6
- net C16_A: track 1761.8 -> 1771.5 mm, vias 5 -> 6
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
